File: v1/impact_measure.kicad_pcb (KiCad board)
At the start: 4 copper layers, 30.6 x 20.5 mm, 63 parts, among them Q2 SP2002KNC, SW1 SW_Push, SW2 SW_Push, U2 ESP32-C3FH4, U3 GS2019-33TR5, U4 ADXL375BCCZ, Y1 40MHz

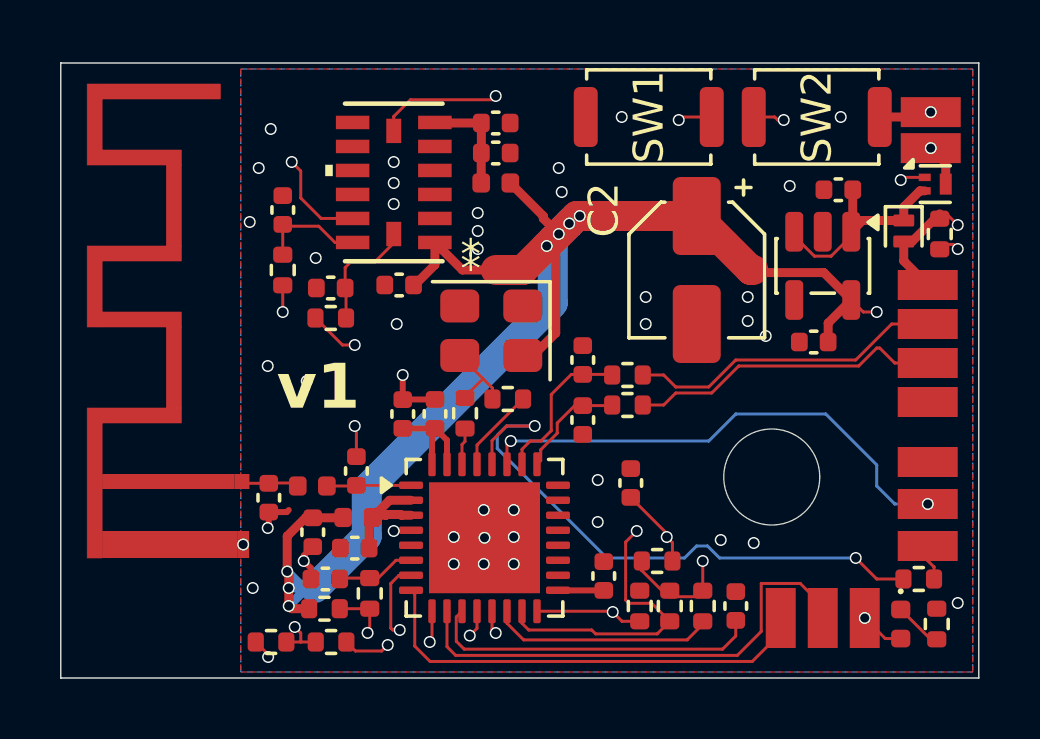
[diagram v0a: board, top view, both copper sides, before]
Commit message: fixed accel land pattern add via fetching increased m3 keepout diameter add int1 and int2 routes fixed wifi track width to 0,35mm moved 10u decap next to ESP32
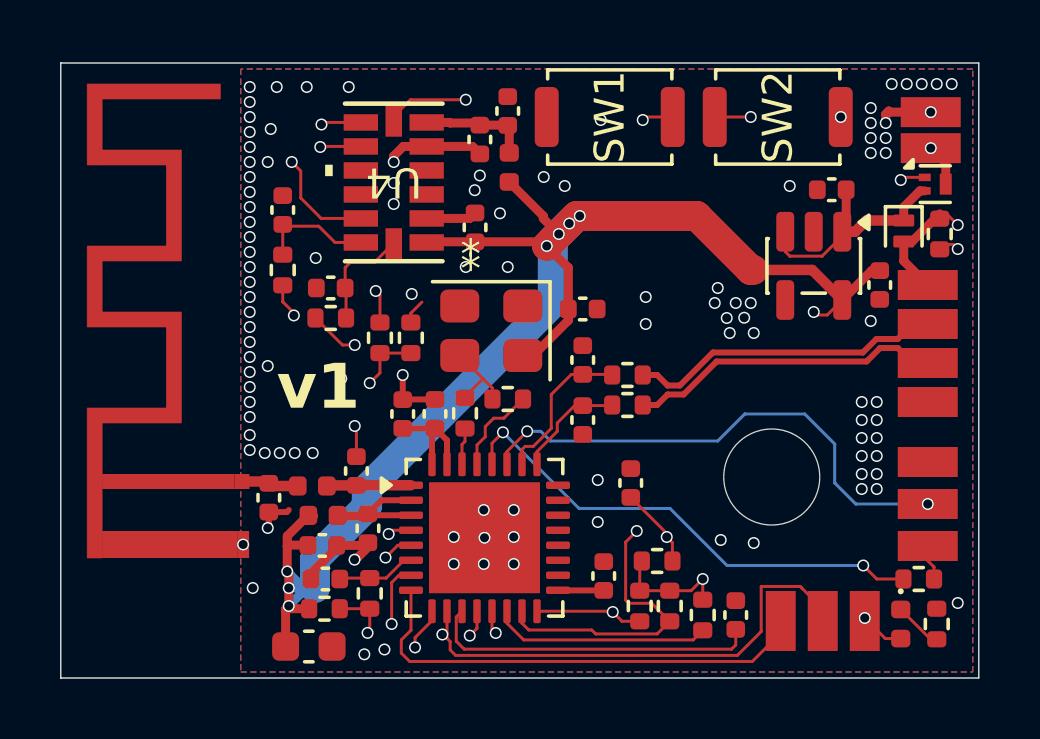
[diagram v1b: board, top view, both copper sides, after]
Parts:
- added C21: 1u, Capacitor_SMD:C_0402_1005Metric, F.Cu at (92.5, 51.8)
- C2: footprint Capacitor_SMD:CP_Elec_4x5.4 -> Capacitor_SMD:C_0603_1608Metric
- U4: footprint Local:LGA_CC-14-1_ADI -> Local:LGA_CC-14-1_ADXL375
- moved C2 18.0 mm to (83.4, 63.0), turned to 0 degrees
- moved R14 10.8 mm to (85.7, 52.8), turned to 90 degrees
- moved R16 10.5 mm to (86.8, 52.8), turned to -90 degrees
- moved C19 3.18 mm to (88.9, 49.1), turned to 90 degrees
- moved C15 2.91 mm to (102.4, 51.0), turned to -90 degrees
- moved SW1 1.30 mm to (93.4, 45.4)
- moved SW2 1.30 mm to (99.0, 45.4)
- moved L1 1.16 mm to (83.8, 58.7)
- moved C1 0.79 mm to (85.3, 59.1), turned to -90 degrees
- moved C20 0.70 mm to (89.1, 46.1), turned to -90 degrees
- moved L3 0.69 mm to (90.0, 47.1), turned to 90 degrees
- moved C18 0.57 mm to (90.0, 45.2), turned to 90 degrees
- moved C3 0.54 mm to (83.8, 59.7), turned to 0 degrees
- moved C6 0.30 mm to (97.6, 62.0)
- moved R3 0.30 mm to (96.5, 62.0)
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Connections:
- R10 pad 1: CLK -> Net-(U4-SCL/SCLK)
- R10 pad 2: Net-(U4-SCL/SCLK) -> CLK
- R11 pad 1: MOSI -> Net-(U4-SDA/SDI/SDIO)
- R11 pad 2: Net-(U4-SDA/SDI/SDIO) -> MOSI
- TP9 pad 1: Net-(U2-MTDI) -> INT1
- U2 pad 10: Net-(U2-MTDI) -> INT1
- U2 pad 5: unconnected-(U2-XTAL_32K_N-Pad5) -> INT2
- U4 pad 8: unconnected-(U4-INT1-Pad8) -> INT1
- U4 pad 9: unconnected-(U4-INT2-Pad9) -> INT2
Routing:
- net INT1: track 0.00 -> 37.6 mm, vias 0 -> 2
- net INT2: track 0.00 -> 17.8 mm, vias 0 -> 2
- net Net-(U2-MTDI): track 16.5 -> 0.00 mm
- net VBAT: track 42.6 -> 27.7 mm
- net GND: track 9.71 -> 15.7 mm, vias 45 -> 109
- net Net-(U2-U0TXD): track 19.9 -> 16.6 mm
- net Net-(U2-LNA_IN): track 2.94 -> 5.75 mm
- net Net-(ANT1-in): track 1.89 -> 3.79 mm
- net Net-(U2-XTAL_32K_P): track 6.77 -> 8.31 mm
- net VDD: track 71.1 -> 69.9 mm
- net MISO: track 23.8 -> 22.8 mm
- net Net-(D1-A): track 17.7 -> 18.5 mm
- net Net-(U2-GPIO3): track 15.2 -> 15.9 mm
- net Net-(D3-K): track 7.44 -> 8.08 mm
- net RESET: track 33.7 -> 33.1 mm
- added copper zone on In1.Cu, net GND
